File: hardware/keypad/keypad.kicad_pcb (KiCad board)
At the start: 2 copper layers, 100 x 100 mm, 26 parts, among them J1 RJ45_Shielded, SW1 SW_Push, SW2 SW_Push, SW3 SW_Push, SW4 SW_Push, U1 WAVGAT_CAN

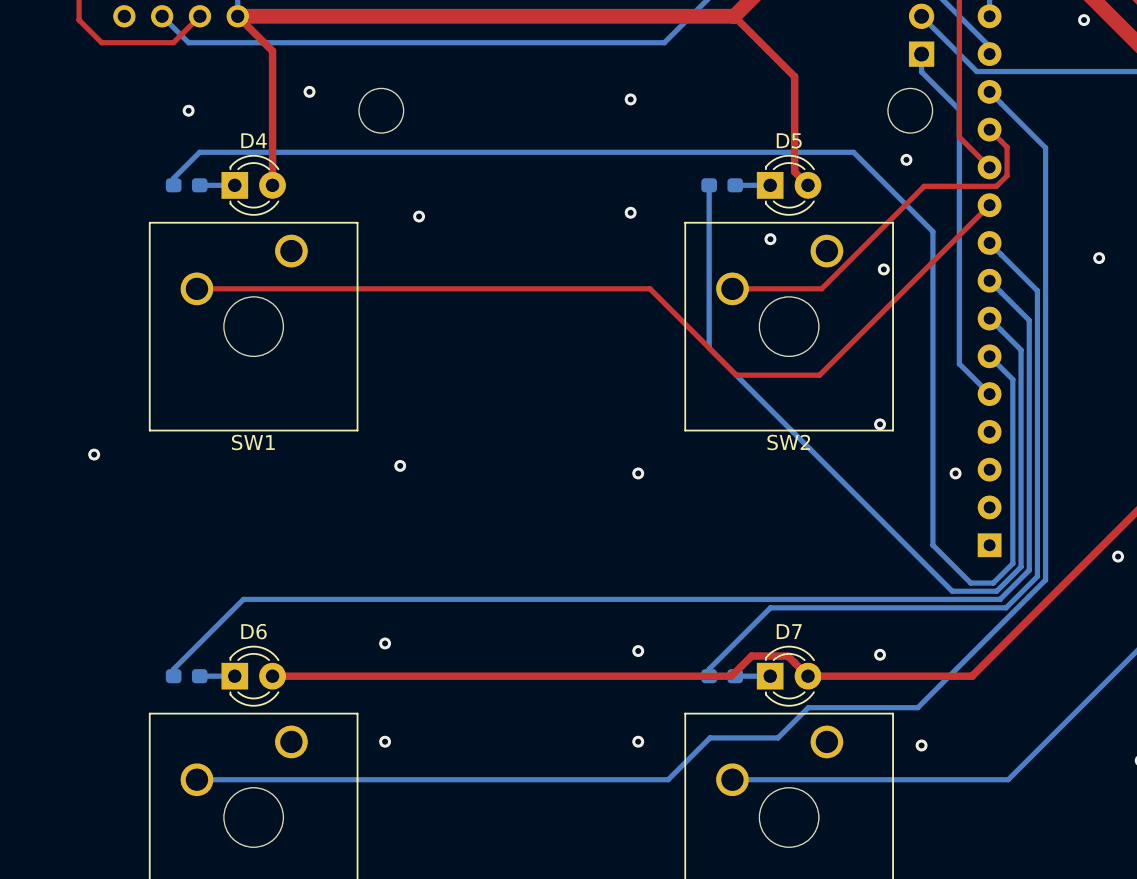
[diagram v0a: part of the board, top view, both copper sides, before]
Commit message: Keypad PCB: add debouncing caps
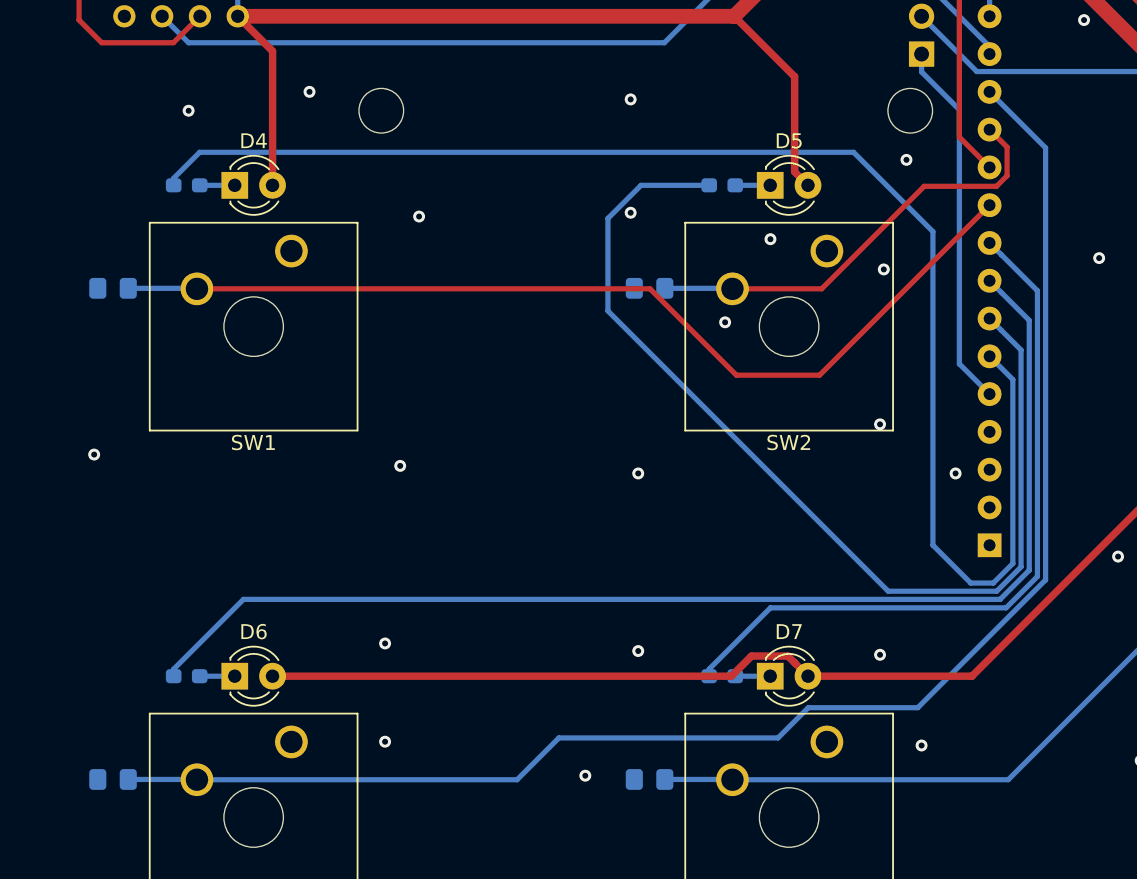
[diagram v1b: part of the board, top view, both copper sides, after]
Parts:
- added C1: C, Capacitor_SMD:C_0805_2012Metric_Pad1.15x1.40mm_HandSolder, B.Cu at (66.5, 90.4)
- added C2: C, Capacitor_SMD:C_0805_2012Metric_Pad1.15x1.40mm_HandSolder, B.Cu at (66.5, 123.4)
- added C3: C, Capacitor_SMD:C_0805_2012Metric_Pad1.15x1.40mm_HandSolder, B.Cu at (102.6, 90.4)
- added C4: C, Capacitor_SMD:C_0805_2012Metric_Pad1.15x1.40mm_HandSolder, B.Cu at (102.6, 123.4)
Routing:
- net D4: track 56.9 -> 67.8 mm
- net D7: track 60.4 -> 65.1 mm
- net D10: track 97.0 -> 101.6 mm
- net D9: track 25.2 -> 29.8 mm
- net A6: track 52.8 -> 57.4 mm
- net GND: vias 45 -> 46

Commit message: Add identifying silkscreen text, fix missing connections on ModuleBase
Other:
- board text added: "BGame Keypad v1.0 PurkkaKoodari 2020"

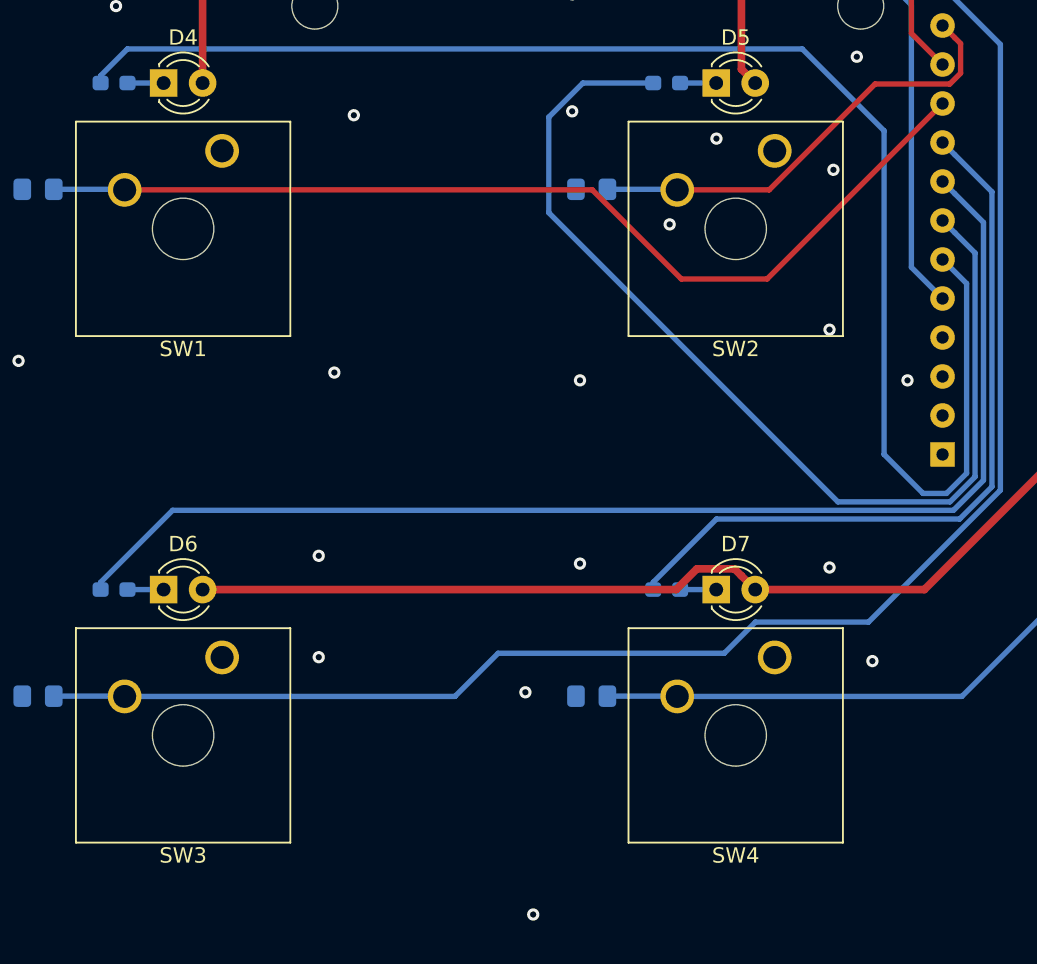
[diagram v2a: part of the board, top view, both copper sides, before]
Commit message: Keypad PCB: add holes for PCB-mounted switches
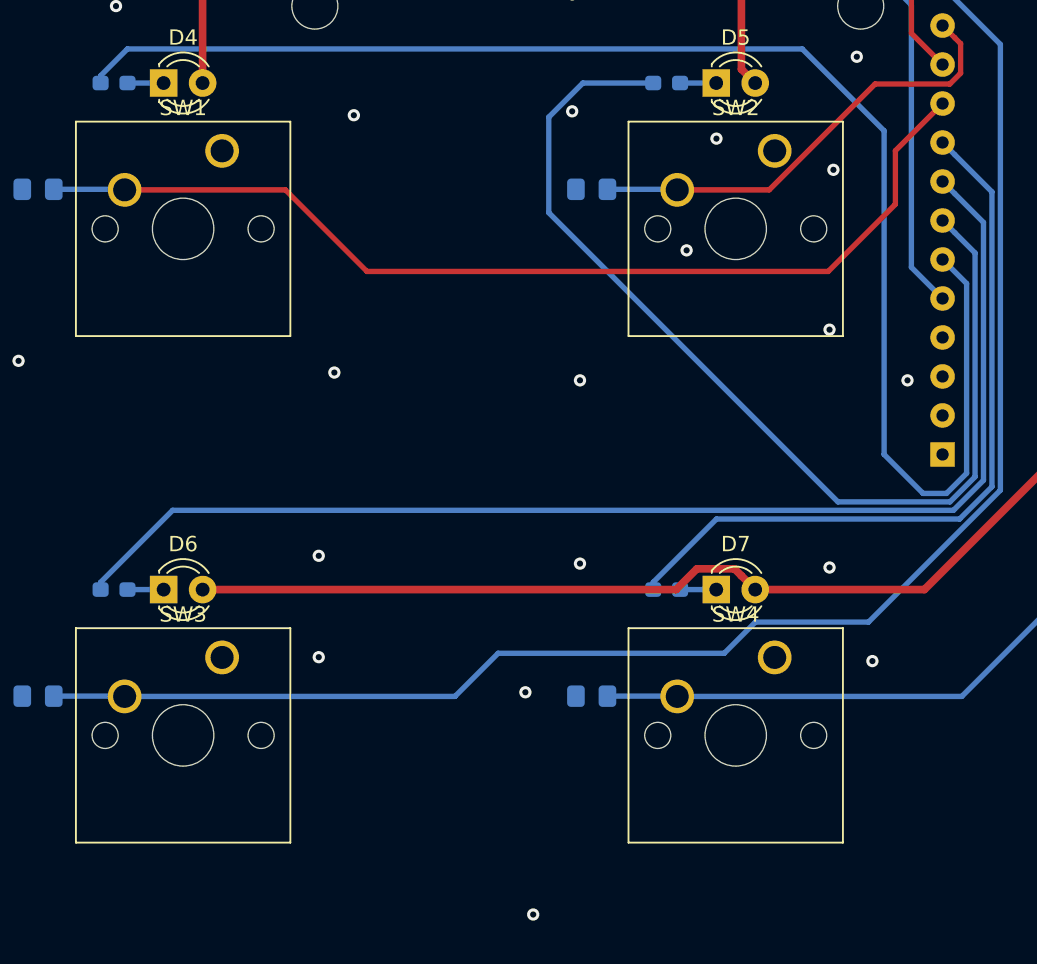
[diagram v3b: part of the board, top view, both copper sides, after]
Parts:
- SW1, SW2, SW3, SW4: footprint Button_Switch_Keyboard:SW_Cherry_MX_1.00u_Plate -> Button_Switch_Keyboard:SW_Cherry_MX_1.00u_PCB
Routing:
- net D7: track 65.1 -> 66.7 mm

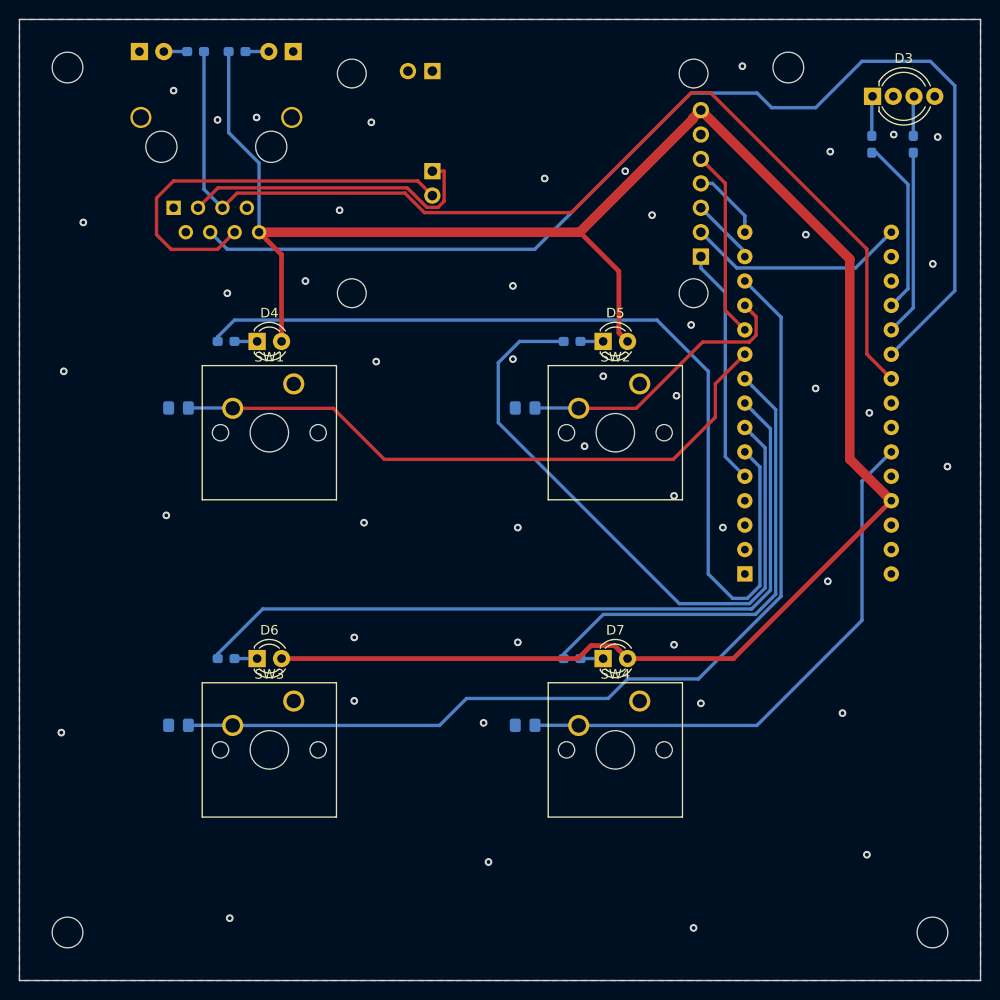
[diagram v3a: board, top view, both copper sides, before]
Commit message: Avoid using D10 (SPI SS) pin as input
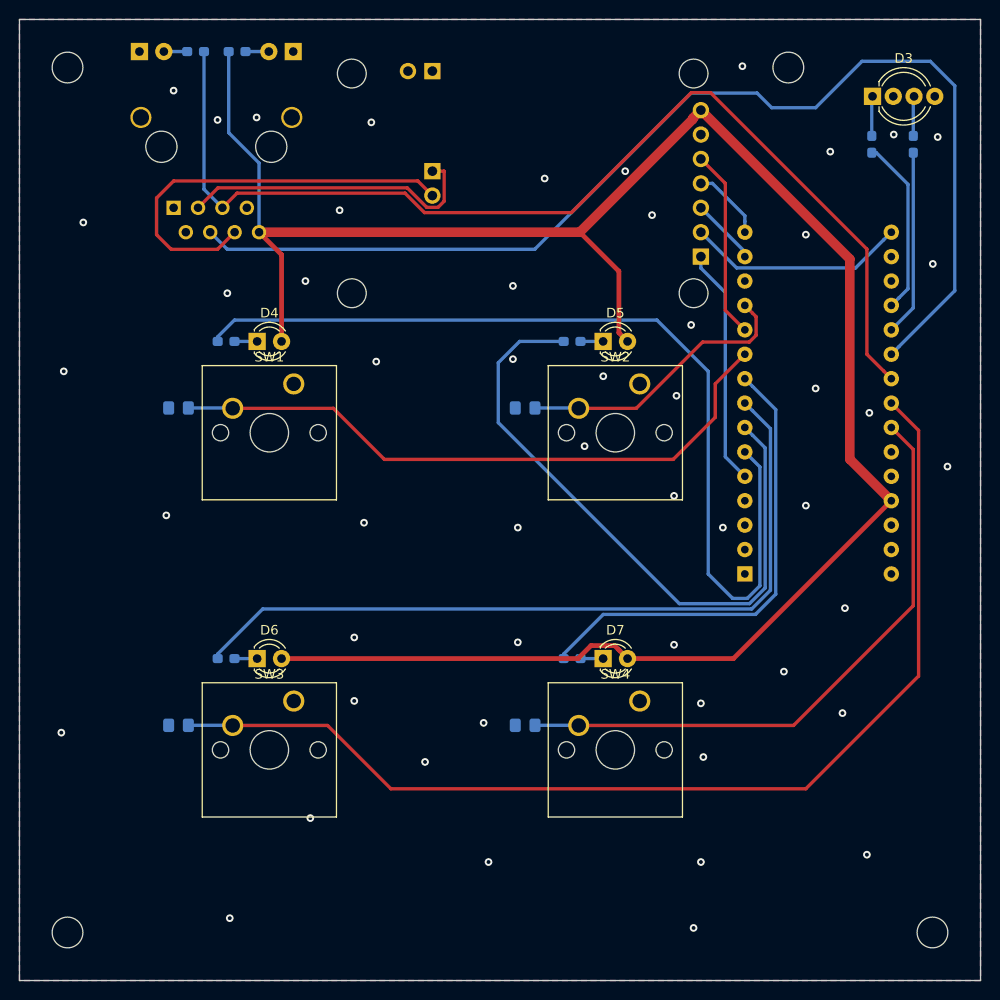
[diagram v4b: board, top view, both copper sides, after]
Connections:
- C2 pad 1: D10 -> A4_SDA
- C4 pad 1: A6 -> A5_SCL
- SW3 pad 2: D10 -> A4_SDA
- SW4 pad 2: A6 -> A5_SCL
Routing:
- net A4_SDA: track 0.00 -> 113.2 mm
- net D10: track 101.6 -> 0.00 mm
- net A5_SCL: track 0.00 -> 64.0 mm
- net A6: track 57.4 -> 0.00 mm
- net GND: vias 46 -> 52

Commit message: Keypad PCB: fix switch positions
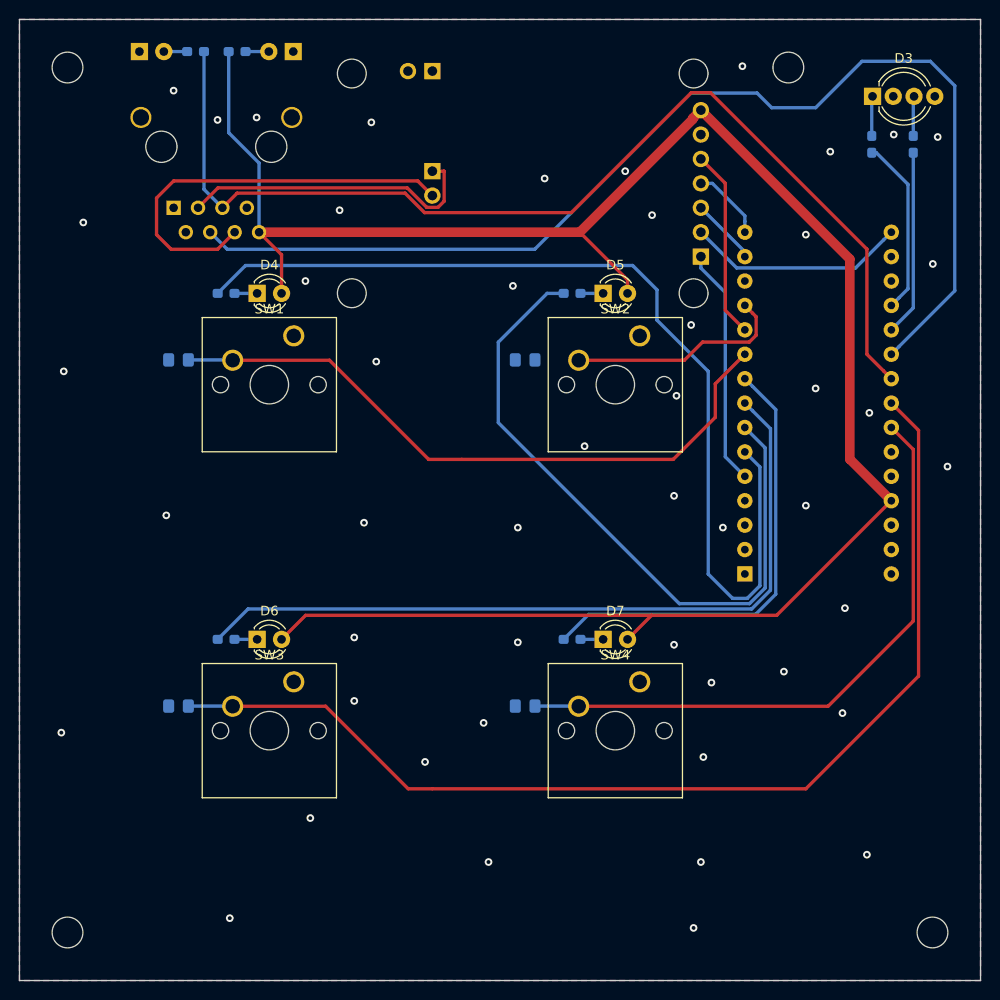
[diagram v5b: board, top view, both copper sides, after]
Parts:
- moved C1 5.00 mm to (66.5, 85.4)
- moved C3 5.00 mm to (102.6, 85.4)
- moved D4 5.00 mm to (74.7, 78.5)
- moved D5 5.00 mm to (110.7, 78.5)
- moved R5 5.00 mm to (71.5, 78.5)
- moved R6 5.00 mm to (107.5, 78.5)
- moved SW1 5.00 mm to (78.5, 82.9)
- moved SW2 5.00 mm to (114.5, 82.9)
- moved C2 2.00 mm to (66.5, 121.4)
- moved C4 2.00 mm to (102.6, 121.4)
- moved D6 2.00 mm to (74.7, 114.5)
- moved D7 2.00 mm to (110.7, 114.5)
- moved R7 2.00 mm to (71.5, 114.5)
- moved R8 2.00 mm to (107.5, 114.5)
- moved SW3 2.00 mm to (78.5, 118.9)
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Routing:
- net VCC: track 217.4 -> 209.0 mm
- net D9: track 29.8 -> 23.1 mm
- net D3: track 97.1 -> 101.3 mm
- net D4: track 67.8 -> 71.1 mm
- net D7: track 66.7 -> 68.8 mm
- net D5: track 81.3 -> 80.2 mm
- net D6: track 48.9 -> 47.8 mm
- net A4_SDA: track 113.2 -> 114.0 mm
- net GND: vias 52 -> 49
- net (no net): vias 0 -> 1
